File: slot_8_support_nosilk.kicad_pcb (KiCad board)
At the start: 2 copper layers, 17.8 x 35.6 mm, 11 parts, among them P6 CONN_1, P7 CONN_1, U1 74LS33

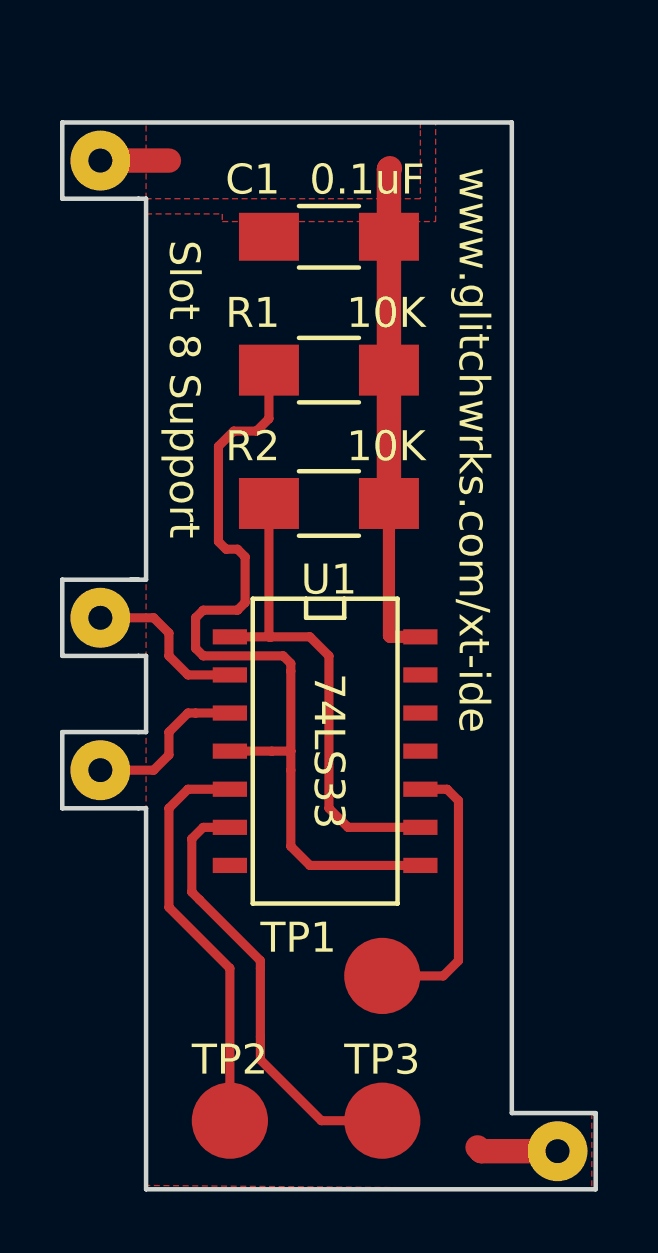
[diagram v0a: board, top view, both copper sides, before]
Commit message: Splitting silkscreen/nosilk boards, adding copper pour for mask relief, bottom mask layer
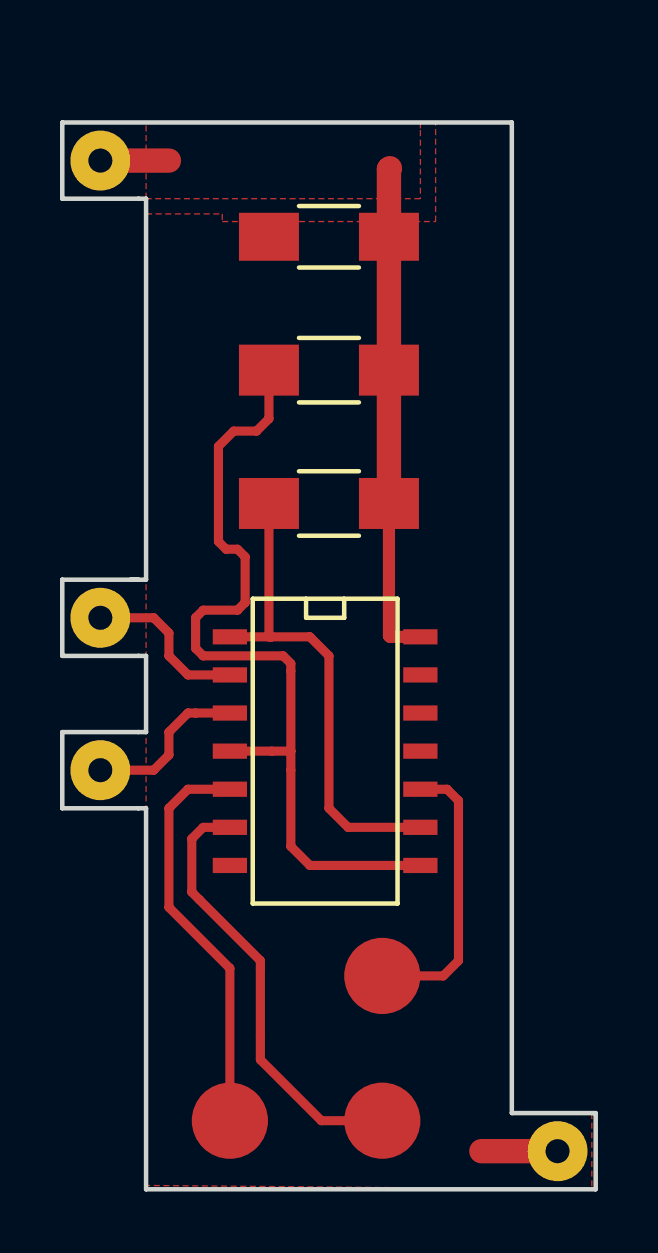
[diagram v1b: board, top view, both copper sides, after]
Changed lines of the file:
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@@
     (area 113.957619 89.581428 136.965 128.858571)
     (thickness 1.6)
-    (drawings 34)
-    (tracks 76)
+    (drawings 31)
+    (tracks 75)
     (zones 0)
     (modules 11)
@@
     (35 F.Paste user)
     (36 B.SilkS user)
-    (37 F.SilkS user)
-    (38 B.Mask user)
+    (37 F.SilkS user hide)
+    (38 B.Mask user hide)
     (39 F.Mask user)
     (40 Dwgs.User user)
@@
     (45 Margin user)
     (46 B.CrtYd user)
-    (47 F.CrtYd user)
+    (47 F.CrtYd user hide)
     (48 B.Fab user)
     (49 F.Fab user)
   )
   (setup
-    (last_trace_width 0.8128)
+    (last_trace_width 0.25)
     (user_trace_width 0.1524)
     (user_trace_width 0.2032)
@@
     (tags "capacitor 1206")
     (attr smd)
-    (fp_text reference C1 (at 2.54 1.905 180) (layer F.SilkS)
-      (effects (font (size 1 1) (thickness 0.15)))
-    )
-    (fp_text value 0.1uF (at -1.27 1.905 180) (layer F.SilkS)
+    (fp_text reference C1 (at 2.54 1.905 180) (layer F.SilkS) hide
+      (effects (font (size 1 1) (thickness 0.15)))
+    )
+    (fp_text value 0.1uF (at -1.27 1.905 180) (layer F.SilkS) hide
       (effects (font (size 1 1) (thickness 0.15)))
     )
@@
     (tags "resistor 1206")
     (attr smd)
-    (fp_text reference R1 (at 2.54 1.905 180) (layer F.SilkS)
-      (effects (font (size 1 1) (thickness 0.15)))
-    )
-    (fp_text value 10K (at -1.905 1.905 180) (layer F.SilkS)
+    (fp_text reference R1 (at 2.54 1.905 180) (layer F.SilkS) hide
+      (effects (font (size 1 1) (thickness 0.15)))
+    )
+    (fp_text value 10K (at -1.905 1.905 180) (layer F.SilkS) hide
       (effects (font (size 1 1) (thickness 0.15)))
     )
@@
     (tags "resistor 1206")
     (attr smd)
-    (fp_text reference R2 (at 2.54 1.905 180) (layer F.SilkS)
-      (effects (font (size 1 1) (thickness 0.15)))
-    )
-    (fp_text value 10K (at -1.905 1.905 180) (layer F.SilkS)
+    (fp_text reference R2 (at 2.54 1.905 180) (layer F.SilkS) hide
+      (effects (font (size 1 1) (thickness 0.15)))
+    )
+    (fp_text value 10K (at -1.905 1.905 180) (layer F.SilkS) hide
       (effects (font (size 1 1) (thickness 0.15)))
     )
@@
     (tags "CMS SOJ")
     (attr smd)
-    (fp_text reference U1 (at -5.715 0 360) (layer F.SilkS)
+    (fp_text reference U1 (at -5.715 0 360) (layer F.SilkS) hide
       (effects (font (size 1 1) (thickness 0.15)))
     )
@@
   (module testpoints:SMD_TESTPOINT (layer F.Cu)
     (at 127.508 119.888)
-    (fp_text reference TP1 (at -2.794 -1.27) (layer F.SilkS)
+    (fp_text reference TP1 (at -2.794 -1.27) (layer F.SilkS) hide
       (effects (font (size 1 1) (thickness 0.15)))
     )
@@
   (module testpoints:SMD_TESTPOINT (layer F.Cu)
     (at 122.428 124.714)
-    (fp_text reference TP2 (at 0 -2.032) (layer F.SilkS)
+    (fp_text reference TP2 (at 0 -2.032) (layer F.SilkS) hide
       (effects (font (size 1 1) (thickness 0.15)))
     )
@@
   (module testpoints:SMD_TESTPOINT (layer F.Cu)
     (at 127.508 124.714)
-    (fp_text reference TP3 (at 0 -2.032) (layer F.SilkS)
+    (fp_text reference TP3 (at 0 -2.032) (layer F.SilkS) hide
       (effects (font (size 1 1) (thickness 0.15)))
     )
@@
     (pad 1 thru_hole circle (at 0 0) (size 1.99898 1.99898) (drill 0.8001) (layers *.Cu *.Mask F.SilkS)
       (net 9 "Net-(/MEMR1-Pad1)"))
-  )
-  (gr_text 74LS33 (at 125.73 112.395 270) (layer F.SilkS)
-    (effects (font (size 1.016 1.016) (thickness 0.1778)))
-  )
-  (gr_text "Slot 8 Support" (at 120.904 100.33 270) (layer F.SilkS)
-    (effects (font (size 1.016 1.016) (thickness 0.1778)))
-  )
-  (gr_text www.glitchwrks.com/xt-ide (at 130.556 102.362 270) (layer F.SilkS)
-    (effects (font (size 1.016 1.016) (thickness 0.1778)))
   )
   (gr_text TP2 (at 120.904 121.412 270) (layer F.Mask)
@@
   (segment (start 127.635 104.775) (end 127.73 104.14) (width 0.4064) (layer F.Cu) (net 1))
   (segment (start 133.35 125.73) (end 130.81 125.73) (width 0.8128) (layer F.Cu) (net 2))
-  (segment (start 130.81 125.73) (end 130.683 125.603) (width 0.8128) (layer F.Cu) (net 2))
   (segment (start 124.206 109.22) (end 121.539 109.22) (width 0.3048) (layer F.Cu) (net 3))
   (segment (start 124.46 109.474) (end 124.206 109.22) (width 0.3048) (layer F.Cu) (net 3))

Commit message: Adding castellated mounting holes for nosilk version
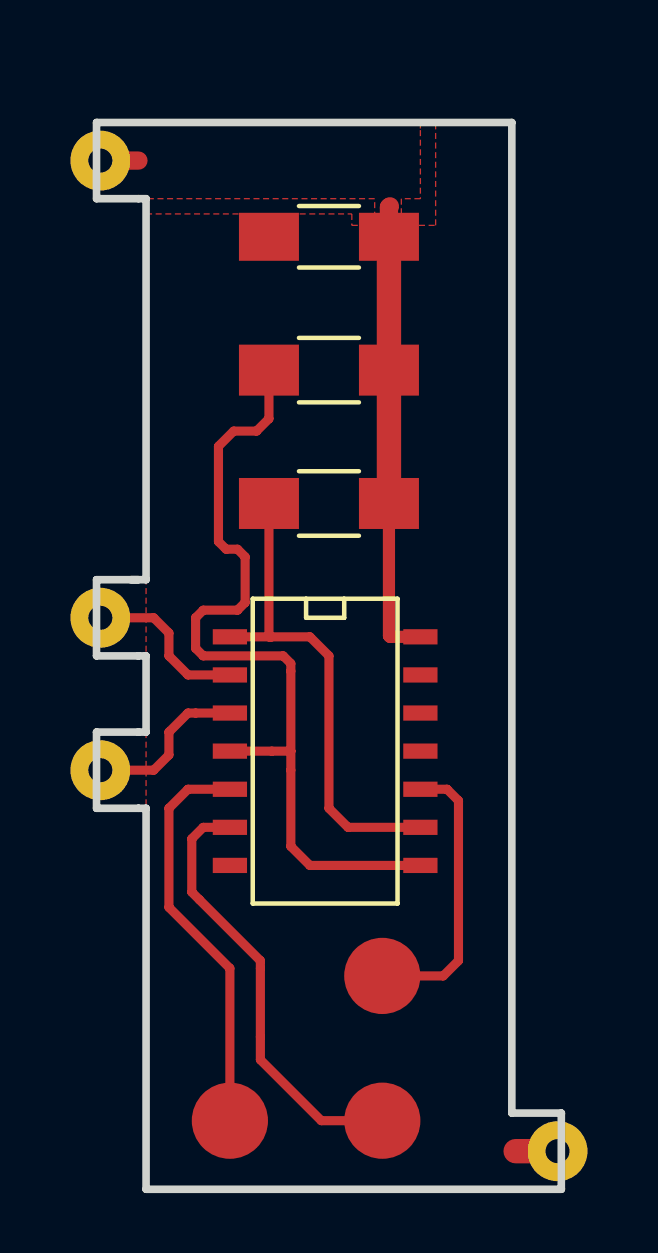
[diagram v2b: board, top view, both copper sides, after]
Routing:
- net VCC: track 19.6 -> 17.3 mm
- net GND: track 2.54 -> 1.40 mm
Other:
- board size 17.8 x 35.6 mm -> 15.5 x 35.6 mm
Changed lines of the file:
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@@
     (35 F.Paste user)
     (36 B.SilkS user)
-    (37 F.SilkS user hide)
+    (37 F.SilkS user)
     (38 B.Mask user hide)
     (39 F.Mask user)
@@
   )
   (setup
-    (last_trace_width 0.25)
+    (last_trace_width 0.3048)
     (user_trace_width 0.1524)
     (user_trace_width 0.2032)
@@
     (mod_text_size 1 1)
     (mod_text_width 0.15)
-    (pad_size 1.524 1.524)
-    (pad_drill 0.762)
+    (pad_size 1.99898 1.99898)
+    (pad_drill 0.8001)
     (pad_to_mask_clearance 0.127)
     (aux_axis_origin 0 0)
@@
       (drillshape 0)
       (scaleselection 1)
-      (outputdirectory gerbers/))
+      (outputdirectory gerbers/nosilk/))
   )
   (net 0 "")
@@
     )
     (pad 1 thru_hole circle (at 0 0 270) (size 1.99898 1.99898) (drill 0.8001) (layers *.Cu *.Mask F.SilkS)
-      (net 2 GND))
+      (net 2 GND) (zone_connect 2))
   )
   (module testpoints:SMD_TESTPOINT (layer F.Cu)
@@
     (effects (font (size 1.016 1.016) (thickness 0.1778)))
   )
-  (gr_line (start 119.634 93.98) (end 119.38 93.98) (angle 90) (layer Edge.Cuts) (width 0.15))
-  (gr_line (start 119.634 106.68) (end 119.126 106.68) (angle 90) (layer Edge.Cuts) (width 0.15))
-  (gr_line (start 119.634 109.22) (end 119.38 109.22) (angle 90) (layer Edge.Cuts) (width 0.15))
-  (gr_line (start 119.634 111.76) (end 119.38 111.76) (angle 90) (layer Edge.Cuts) (width 0.15))
-  (gr_line (start 119.634 114.3) (end 119.38 114.3) (angle 90) (layer Edge.Cuts) (width 0.15))
-  (gr_line (start 134.62 127) (end 119.634 127) (angle 90) (layer Edge.Cuts) (width 0.15))
-  (gr_line (start 134.62 127) (end 134.62 124.46) (angle 90) (layer Edge.Cuts) (width 0.15))
-  (gr_line (start 119.634 114.3) (end 119.634 127) (angle 90) (layer Edge.Cuts) (width 0.15))
-  (gr_line (start 116.84 114.3) (end 119.38 114.3) (angle 90) (layer Edge.Cuts) (width 0.15))
-  (gr_line (start 116.84 111.76) (end 116.84 114.3) (angle 90) (layer Edge.Cuts) (width 0.15))
-  (gr_line (start 119.38 111.76) (end 116.84 111.76) (angle 90) (layer Edge.Cuts) (width 0.15))
-  (gr_line (start 119.634 109.22) (end 119.634 111.76) (angle 90) (layer Edge.Cuts) (width 0.15))
-  (gr_line (start 116.84 109.22) (end 119.38 109.22) (angle 90) (layer Edge.Cuts) (width 0.15))
-  (gr_line (start 116.84 106.68) (end 116.84 109.22) (angle 90) (layer Edge.Cuts) (width 0.15))
-  (gr_line (start 119.38 106.68) (end 116.84 106.68) (angle 90) (layer Edge.Cuts) (width 0.15))
-  (gr_line (start 119.634 93.98) (end 119.634 106.68) (angle 90) (layer Edge.Cuts) (width 0.15))
-  (gr_line (start 116.84 93.98) (end 119.38 93.98) (angle 90) (layer Edge.Cuts) (width 0.15))
-  (gr_line (start 116.84 91.44) (end 116.84 93.98) (angle 90) (layer Edge.Cuts) (width 0.15))
-  (gr_line (start 131.826 91.44) (end 116.84 91.44) (angle 90) (layer Edge.Cuts) (width 0.15))
-  (gr_line (start 131.826 124.46) (end 131.826 91.44) (angle 90) (layer Edge.Cuts) (width 0.15))
-  (gr_line (start 134.62 124.46) (end 131.826 124.46) (angle 90) (layer Edge.Cuts) (width 0.15))
-  (segment (start 127.73 95.25) (end 127.73 92.996) (width 0.8128) (layer F.Cu) (net 1))
-  (segment (start 127.73 92.996) (end 127.762 92.964) (width 0.8128) (layer F.Cu) (net 1))
-  (segment (start 118.11 92.71) (end 120.396 92.71) (width 0.8128) (layer F.Cu) (net 1))
+  (gr_line (start 119.634 93.98) (end 119.38 93.98) (angle 90) (layer Edge.Cuts) (width 0.254))
+  (gr_line (start 119.634 106.68) (end 119.126 106.68) (angle 90) (layer Edge.Cuts) (width 0.254))
+  (gr_line (start 119.634 109.22) (end 119.38 109.22) (angle 90) (layer Edge.Cuts) (width 0.254))
+  (gr_line (start 119.634 111.76) (end 119.38 111.76) (angle 90) (layer Edge.Cuts) (width 0.254))
+  (gr_line (start 119.634 114.3) (end 119.38 114.3) (angle 90) (layer Edge.Cuts) (width 0.254))
+  (gr_line (start 133.477 127) (end 119.634 127) (angle 90) (layer Edge.Cuts) (width 0.254))
+  (gr_line (start 133.477 127) (end 133.477 124.46) (angle 90) (layer Edge.Cuts) (width 0.254))
+  (gr_line (start 119.634 114.3) (end 119.634 127) (angle 90) (layer Edge.Cuts) (width 0.254))
+  (gr_line (start 117.983 114.3) (end 119.38 114.3) (angle 90) (layer Edge.Cuts) (width 0.254))
+  (gr_line (start 117.983 111.76) (end 117.983 114.3) (angle 90) (layer Edge.Cuts) (width 0.254))
+  (gr_line (start 119.38 111.76) (end 117.983 111.76) (angle 90) (layer Edge.Cuts) (width 0.254))
+  (gr_line (start 119.634 109.22) (end 119.634 111.76) (angle 90) (layer Edge.Cuts) (width 0.254))
+  (gr_line (start 117.983 109.22) (end 119.38 109.22) (angle 90) (layer Edge.Cuts) (width 0.254))
+  (gr_line (start 117.983 106.68) (end 117.983 109.22) (angle 90) (layer Edge.Cuts) (width 0.254))
+  (gr_line (start 119.38 106.68) (end 117.983 106.68) (angle 90) (layer Edge.Cuts) (width 0.254))
+  (gr_line (start 119.634 93.98) (end 119.634 106.68) (angle 90) (layer Edge.Cuts) (width 0.254))
+  (gr_line (start 117.983 93.98) (end 119.38 93.98) (angle 90) (layer Edge.Cuts) (width 0.254))
+  (gr_line (start 117.983 91.44) (end 117.983 93.98) (angle 90) (layer Edge.Cuts) (width 0.254))
+  (gr_line (start 131.826 91.44) (end 117.983 91.44) (angle 90) (layer Edge.Cuts) (width 0.254))
+  (gr_line (start 131.826 124.46) (end 131.826 91.44) (angle 90) (layer Edge.Cuts) (width 0.254))
+  (gr_line (start 133.477 124.46) (end 131.826 124.46) (angle 90) (layer Edge.Cuts) (width 0.254))
+  (segment (start 118.11 92.71) (end 119.38 92.71) (width 0.6096) (layer F.Cu) (net 1))
+  (segment (start 127.73 95.25) (end 127.73 94.266) (width 0.6096) (layer F.Cu) (net 1))
+  (segment (start 127.73 94.266) (end 127.762 94.234) (width 0.6096) (layer F.Cu) (net 1))
   (segment (start 127.73 99.695) (end 127.73 95.25) (width 0.8128) (layer F.Cu) (net 1))
   (segment (start 127.73 104.14) (end 127.73 99.695) (width 0.8128) (layer F.Cu) (net 1))
@@
   (segment (start 127.73 108.553) (end 127.73 104.14) (width 0.4064) (layer F.Cu) (net 1))
   (segment (start 127.635 104.775) (end 127.73 104.14) (width 0.4064) (layer F.Cu) (net 1))
-  (segment (start 133.35 125.73) (end 130.81 125.73) (width 0.8128) (layer F.Cu) (net 2))
+  (segment (start 133.35 125.73) (end 131.953 125.73) (width 0.8128) (layer F.Cu) (net 2))
   (segment (start 124.206 109.22) (end 121.539 109.22) (width 0.3048) (layer F.Cu) (net 3))
   (segment (start 124.46 109.474) (end 124.206 109.22) (width 0.3048) (layer F.Cu) (net 3))
@@
   (segment (start 125.476 124.714) (end 127.508 124.714) (width 0.3048) (layer F.Cu) (net 7))
   (segment (start 123.444 122.682) (end 125.476 124.714) (width 0.3048) (layer F.Cu) (net 7))
+  (segment (start 120.396 111.76) (end 120.396 112.522) (width 0.3048) (layer F.Cu) (net 8))
+  (segment (start 120.396 112.522) (end 119.888 113.03) (width 0.3048) (layer F.Cu) (net 8))
+  (segment (start 119.888 113.03) (end 118.11 113.03) (width 0.3048) (layer F.Cu) (net 8))
+  (segment (start 121.031 111.125) (end 120.396 111.76) (width 0.3048) (layer F.Cu) (net 8))
+  (segment (start 122.428 111.125) (end 121.285 111.125) (width 0.3048) (layer F.Cu) (net 8))
   (segment (start 121.285 111.125) (end 121.031 111.125) (width 0.3048) (layer F.Cu) (net 8))
-  (segment (start 122.428 111.125) (end 121.285 111.125) (width 0.3048) (layer F.Cu) (net 8))
-  (segment (start 119.888 113.03) (end 118.11 113.03) (width 0.3048) (layer F.Cu) (net 8))
-  (segment (start 120.396 112.522) (end 119.888 113.03) (width 0.3048) (layer F.Cu) (net 8))
-  (segment (start 120.396 111.76) (end 120.396 112.522) (width 0.3048) (layer F.Cu) (net 8))
-  (segment (start 121.031 111.125) (end 120.396 111.76) (width 0.3048) (layer F.Cu) (net 8))
+  (segment (start 120.396 108.458) (end 119.888 107.95) (width 0.3048) (layer F.Cu) (net 9))
+  (segment (start 119.888 107.95) (end 118.11 107.95) (width 0.3048) (layer F.Cu) (net 9))
+  (segment (start 121.031 109.855) (end 120.396 109.22) (width 0.3048) (layer F.Cu) (net 9))
+  (segment (start 120.396 109.22) (end 120.396 108.458) (width 0.3048) (layer F.Cu) (net 9))
   (segment (start 122.428 109.855) (end 121.031 109.855) (width 0.3048) (layer F.Cu) (net 9))
-  (segment (start 119.888 107.95) (end 118.11 107.95) (width 0.3048) (layer F.Cu) (net 9))
-  (segment (start 120.396 108.458) (end 119.888 107.95) (width 0.3048) (layer F.Cu) (net 9))
-  (segment (start 120.396 109.22) (end 120.396 108.458) (width 0.3048) (layer F.Cu) (net 9))
-  (segment (start 121.031 109.855) (end 120.396 109.22) (width 0.3048) (layer F.Cu) (net 9))
   (zone (net 2) (net_name GND) (layer F.Cu) (hatch edge 0.508)
     (connect_pads (clearance 0.254))
@@
     (polygon
       (pts
-        (xy 131.826 124.46) (xy 134.493 124.46) (xy 134.493 127) (xy 119.634 126.873) (xy 119.634 94.488)
-        (xy 122.174 94.488) (xy 122.174 94.742) (xy 129.286 94.742) (xy 129.286 91.44) (xy 131.826 91.44)
+        (xy 131.826 124.46) (xy 133.477 124.46) (xy 133.477 127) (xy 119.634 127) (xy 119.634 94.488)
+        (xy 126.492 94.488) (xy 126.492 94.869) (xy 129.286 94.869) (xy 129.286 91.44) (xy 131.826 91.44)
       )
     )
   )
   (zone (net 1) (net_name VCC) (layer F.Cu) (hatch edge 0.508)
-    (connect_pads (clearance 0.254))
+    (connect_pads yes (clearance 0.254))
     (min_thickness 0.254)
-    (fill yes (arc_segments 16) (thermal_gap 0.508) (thermal_bridge_width 0.508))
+    (fill yes (arc_segments 16) (thermal_gap 0) (thermal_bridge_width 0.508))
     (polygon
       (pts
-        (xy 128.778 93.98) (xy 119.634 93.98) (xy 119.634 91.44) (xy 128.778 91.44) (xy 128.778 91.694)
+        (xy 128.778 93.98) (xy 128.143 93.98) (xy 128.143 94.615) (xy 127.254 94.615) (xy 127.254 93.98)
+        (xy 117.983 93.98) (xy 117.983 91.44) (xy 128.778 91.44) (xy 128.778 91.694)
       )
     )
